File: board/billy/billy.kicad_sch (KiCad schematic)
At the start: 83 parts, among them J1 Screw_Terminal_01x02, J10 Screw_Terminal_01x02, J11 Screw_Terminal_01x03, J12 USB_B_Micro, J2 Conn_01x06, J3 Screw_Terminal_01x02, J4 Screw_Terminal_01x02, J5 Conn_01x02, J6 Conn_01x03, J7 Screw_Terminal_01x02, J8 Screw_Terminal_01x02, J9 Screw_Terminal_01x02, Q1 AOSS32334C, Q2 AOSS32334C, Q3 AOSS32334C, Q4 AOSS32334C, SW1 TS-1088-AR02016, U1 ESP32-S3-WROOM-1, U2 DRV8833PWPR, U3 MAX98357A, U4 DRV8833PWPR, U5 LM74700-Q1, U6 AP63203WU, U7 USBLC6-2SC6, U8 LM74700-Q1, U9 LM74700-Q1

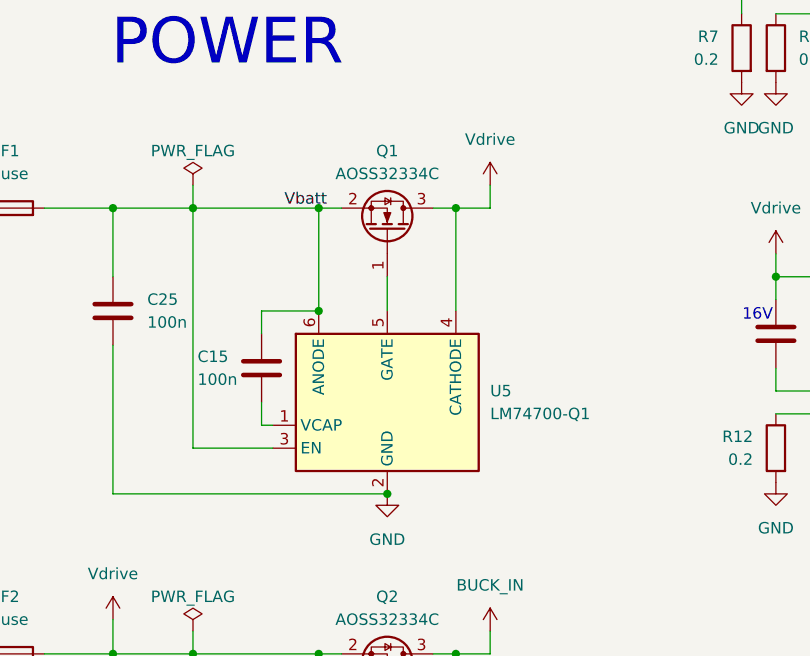
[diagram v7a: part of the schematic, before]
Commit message: Replace battery-leg ideal diode with passive P-FET reverse-polarity protection
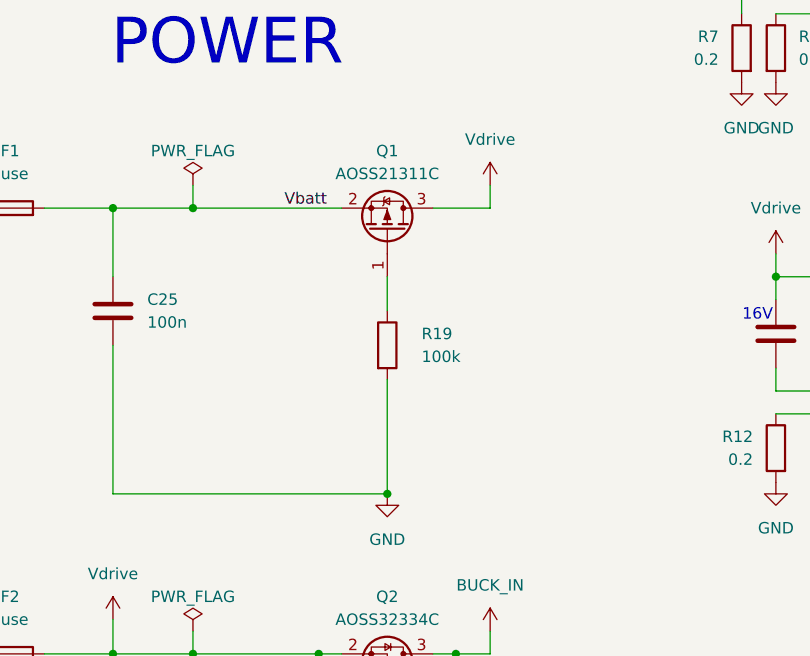
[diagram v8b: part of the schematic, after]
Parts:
- removed C15: 100n, Capacitor_SMD:C_0603_1608Metric, symbol Device:C
- removed U5: LM74700-Q1, Package_TO_SOT_SMD:SOT-23-6, symbol Power_Management:LM74700
- added R19: 100k, Resistor_SMD:R_0603_1608Metric, symbol Device:R
- Q1: value AOSS32334C -> AOSS21311C; symbol Transistor_FET:AO3400A -> Transistor_FET:AO3401A; DigiKey Part 785-AOSS32334CCT-ND -> 785-AOSS21311CCT-ND; LCSC Part C3280157 -> C3280149; MP AOSS32334C -> AOSS21311C
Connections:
- net GND: now also R19.2
- net at Q1.1 (G): now also R19.1
